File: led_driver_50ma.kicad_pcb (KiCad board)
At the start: 2 copper layers, 16 x 22.5 mm, 6 parts, among them J1 USB Micro B, J2 Screw_Terminal_01x02, SW2 Slide Switch

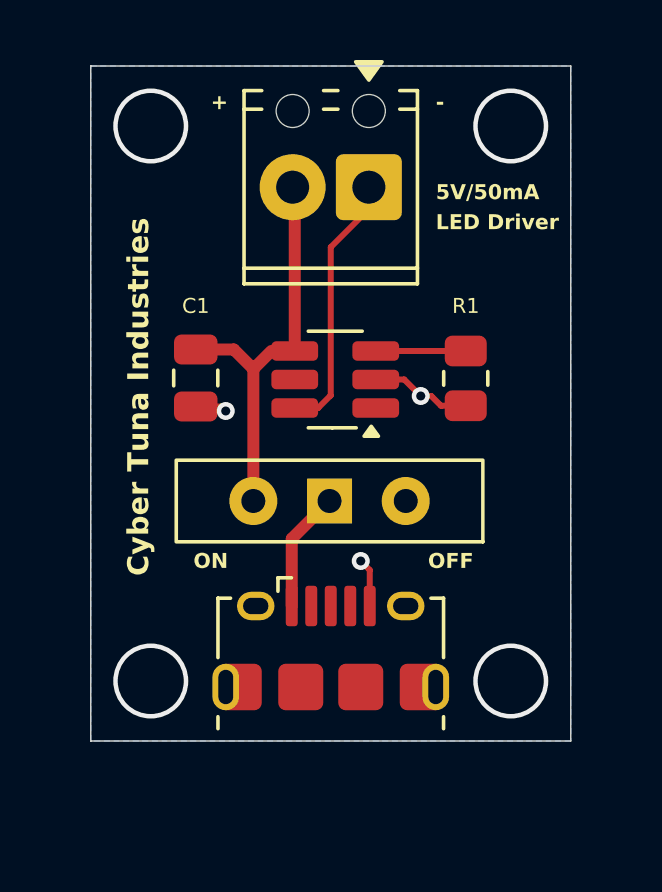
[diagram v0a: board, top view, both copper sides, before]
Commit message: Use bottom layer ground pour and few other tweaks
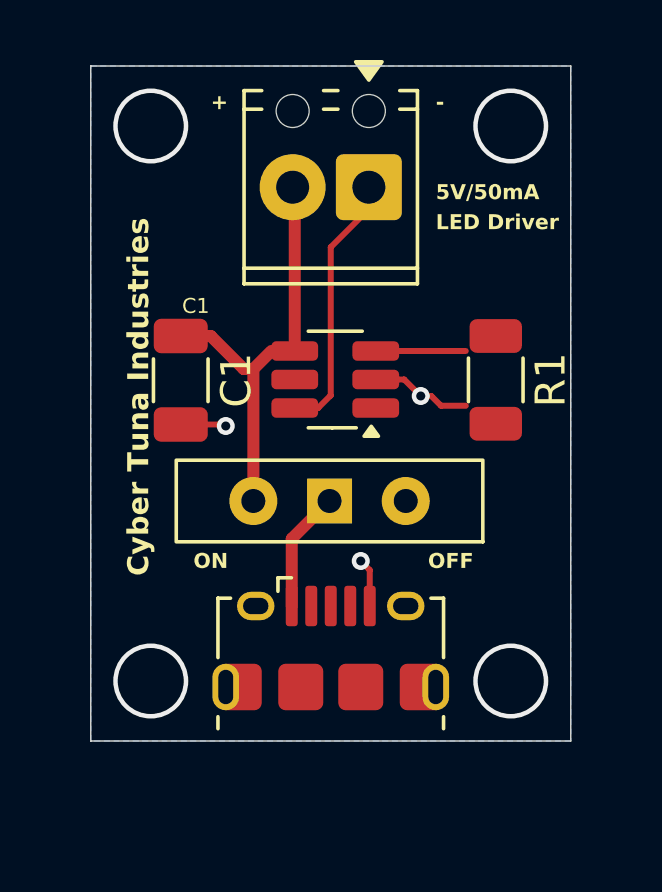
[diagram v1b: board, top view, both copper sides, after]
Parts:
- C1: footprint Capacitor_SMD:C_0805_2012Metric -> Capacitor_SMD:C_1206_3216Metric
- R1: footprint Resistor_SMD:R_0805_2012Metric -> Resistor_SMD:R_1206_3216Metric
- U1: value ~ -> AL5819
- moved R1 1.00 mm to (142.0, 104.5)
- moved C1 0.51 mm to (131.5, 104.5)
- renumbered SW2 to SW1
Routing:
- net +5V: track 13.4 -> 14.1 mm
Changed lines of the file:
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@@
 	(net 10 "unconnected-(U1-NC-Pad5)")
 	(net 11 "Net-(J1-VBUS)")
-	(net 12 "unconnected-(SW2-C-Pad2)")
+	(net 12 "unconnected-(SW1-C-Pad2)")
 	(footprint "Connector_USB:USB_Micro-B_Amphenol_10118194-0001LF_Horizontal"
 		(layer "F.Cu")
@@
 			)
 		)
-		(property "Value" "~"
+		(property "Value" "AL5819"
 			(at 0 2.9 0)
 			(layer "F.Fab")
@@
 		)
 	)
-	(footprint "Resistor_SMD:R_0805_2012Metric"
-		(layer "F.Cu")
-		(at 141 104.4125 -90)
-		(descr "Resistor SMD 0805 (2012 Metric), square (rectangular) end terminal, IPC-7351 nominal, (Body size source: IPC-SM-782 page 72, https://www.pcb-3d.com/wordpress/wp-content/uploads/ipc-sm-782a_amendment_1_and_2.pdf), generated with kicad-footprint-generator")
+	(footprint "Resistor_SMD:R_1206_3216Metric"
+		(layer "F.Cu")
+		(at 142 104.4625 -90)
+		(descr "Resistor SMD 1206 (3216 Metric), square (rectangular) end terminal, IPC-7351 nominal, (Body size source: IPC-SM-782 page 72, https://www.pcb-3d.com/wordpress/wp-content/uploads/ipc-sm-782a_amendment_1_and_2.pdf), generated with kicad-footprint-generator")
 		(tags "resistor")
 		(property "Reference" "R1"
-			(at -2.4125 0 180)
-			(layer "F.SilkS")
-			(effects
-				(font
-					(size 0.5 0.5)
-					(thickness 0.0625)
+			(at 0 -1.83 270)
+			(layer "F.SilkS")
+			(effects
+				(font
+					(size 1 1)
+					(thickness 0.15)
 				)
 			)
 		)
 		(property "Value" "30K"
-			(at 0 1.65 90)
-			(layer "F.Fab")
-			(hide yes)
+			(at 0 1.83 270)
+			(layer "F.Fab")
 			(effects
 				(font
@@
 		)
 		(property "Datasheet" "~"
-			(at 0 0 90)
+			(at 0 0 270)
 			(layer "F.Fab")
 			(hide yes)
@@
 		)
 		(property "Description" "Resistor, US symbol"
-			(at 0 0 90)
+			(at 0 0 270)
 			(layer "F.Fab")
 			(hide yes)
@@
 		(attr smd)
 		(fp_line
-			(start -0.227064 0.735)
-			(end 0.227064 0.735)
-			(stroke
-				(width 0.12)
-				(type solid)
-			)
-			(layer "F.SilkS")
-		)
-		(fp_line
-			(start -0.227064 -0.735)
-			(end 0.227064 -0.735)
+			(start -0.727064 0.91)
+			(end 0.727064 0.91)
+			(stroke
+				(width 0.12)
+				(type solid)
+			)
+			(layer "F.SilkS")
+		)
+		(fp_line
+			(start -0.727064 -0.91)
+			(end 0.727064 -0.91)
 			(stroke
 				(width 0.12)
@@
 		)
 		(fp_rect
-			(start -1.68 -0.95)
-			(end 1.68 0.95)
+			(start -2.28 -1.13)
+			(end 2.28 1.13)
 			(stroke
 				(width 0.05)
@@
 		)
 		(fp_rect
-			(start -1 -0.625)
-			(end 1 0.625)
+			(start -1.6 -0.8)
+			(end 1.6 0.8)
 			(stroke
 				(width 0.1)
@@
 		)
 		(fp_text user "${REFERENCE}"
-			(at 0 0 90)
-			(layer "F.Fab")
-			(effects
-				(font
-					(size 0.5 0.5)
-					(thickness 0.08)
+			(at 0 0 270)
+			(layer "F.Fab")
+			(effects
+				(font
+					(size 0.8 0.8)
+					(thickness 0.12)
 				)
 			)
 		)
 		(pad "1" smd roundrect
-			(at -0.9125 0 270)
-			(size 1.025 1.4)
-			(layers "F.Cu" "F.Mask" "F.Paste")
-			(roundrect_rratio 0.243902)
+			(at -1.4625 0 270)
+			(size 1.125 1.75)
+			(layers "F.Cu" "F.Mask" "F.Paste")
+			(roundrect_rratio 0.222222)
 			(net 8 "Net-(U1-R_{SET})")
 			(pintype "passive")
 		)
 		(pad "2" smd roundrect
-			(at 0.9125 0 270)
-			(size 1.025 1.4)
-			(layers "F.Cu" "F.Mask" "F.Paste")
-			(roundrect_rratio 0.243902)
+			(at 1.4625 0 270)
+			(size 1.125 1.75)
+			(layers "F.Cu" "F.Mask" "F.Paste")
+			(roundrect_rratio 0.222222)
 			(net 1 "GND")
 			(pintype "passive")
 		)
 		(embedded_fonts no)
-		(model "${KICAD9_3DMODEL_DIR}/Resistor_SMD.3dshapes/R_0805_2012Metric.step"
+		(model "${KICAD9_3DMODEL_DIR}/Resistor_SMD.3dshapes/R_1206_3216Metric.step"
 			(offset
 				(xyz 0 0 0)
@@
 		(descr "Wuerth, WS-SLTV, 450301014042, https://www.we-online.com/components/products/datasheet/450301014042.pdf")
 		(tags "switch single-pole opposite-side-connection double-throw SPDT würth wurth")
-		(property "Reference" "SW2"
+		(property "Reference" "SW1"
 			(at 5.96 -5 0)
 			(layer "F.SilkS")
@@
 			(layers "*.Cu" "*.Mask")
 			(remove_unused_layers no)
-			(net 12 "unconnected-(SW2-C-Pad2)")
+			(net 12 "unconnected-(SW1-C-Pad2)")
 			(pinfunction "C")
 			(pintype "passive")
@@
 		)
 	)
-	(footprint "Capacitor_SMD:C_0805_2012Metric"
-		(layer "F.Cu")
-		(at 132 104.4 -90)
-		(descr "Capacitor SMD 0805 (2012 Metric), square (rectangular) end terminal, IPC-7351 nominal, (Body size source: IPC-SM-782 page 76, https://www.pcb-3d.com/wordpress/wp-content/uploads/ipc-sm-782a_amendment_1_and_2.pdf, https://docs.google.com/spreadsheets/d/1BsfQQcO9C6DZCsRaXUlFlo91Tg2WpOkGARC1WS5S8t0/edit?usp=sharing), generated with kicad-footprint-generator")
+	(footprint "Capacitor_SMD:C_1206_3216Metric"
+		(layer "F.Cu")
+		(at 131.5 104.475 -90)
+		(descr "Capacitor SMD 1206 (3216 Metric), square (rectangular) end terminal, IPC-7351 nominal, (Body size source: IPC-SM-782 page 76, https://www.pcb-3d.com/wordpress/wp-content/uploads/ipc-sm-782a_amendment_1_and_2.pdf), generated with kicad-footprint-generator")
 		(tags "capacitor")
 		(property "Reference" "C1"
-			(at -2.9 0 90)
-			(layer "F.SilkS")
-			(hide yes)
+			(at 0 -1.85 270)
+			(layer "F.SilkS")
 			(effects
 				(font
@@
 		)
 		(property "Value" "1uF"
-			(at 0 1.68 90)
-			(layer "F.Fab")
-			(hide yes)
+			(at 0 1.85 270)
+			(layer "F.Fab")
 			(effects
 				(font
@@
 		)
 		(property "Datasheet" ""
-			(at 0 0 90)
+			(at 0 0 270)
 			(layer "F.Fab")
 			(hide yes)
@@
 		)
 		(property "Description" "capacitor, small US symbol"
-			(at 0 0 90)
+			(at 0 0 270)
 			(layer "F.Fab")
 			(hide yes)
@@
 		(attr smd)
 		(fp_line
-			(start -0.261252 0.735)
-			(end 0.261252 0.735)
-			(stroke
-				(width 0.12)
-				(type solid)
-			)
-			(layer "F.SilkS")
-		)
-		(fp_line
-			(start -0.261252 -0.735)
-			(end 0.261252 -0.735)
+			(start -0.711252 0.91)
+			(end 0.711252 0.91)
+			(stroke
+				(width 0.12)
+				(type solid)
+			)
+			(layer "F.SilkS")
+		)
+		(fp_line
+			(start -0.711252 -0.91)
+			(end 0.711252 -0.91)
 			(stroke
 				(width 0.12)
@@
 		)
 		(fp_rect
-			(start -1.7 -0.98)
-			(end 1.7 0.98)
+			(start -2.3 -1.15)
+			(end 2.3 1.15)
 			(stroke
 				(width 0.05)
@@
 		)
 		(fp_rect
-			(start -1 -0.625)
-			(end 1 0.625)
+			(start -1.6 -0.8)
+			(end 1.6 0.8)
 			(stroke
 				(width 0.1)
@@
 		)
 		(fp_text user "${REFERENCE}"
-			(at 0 0 90)
-			(layer "F.Fab")
-			(effects
-				(font
-					(size 0.5 0.5)
-					(thickness 0.08)
+			(at 0 0 270)
+			(layer "F.Fab")
+			(effects
+				(font
+					(size 0.8 0.8)
+					(thickness 0.12)
 				)
 			)
 		)
 		(pad "1" smd roundrect
-			(at -0.95 0 270)
-			(size 1 1.45)
-			(layers "F.Cu" "F.Mask" "F.Paste")
-			(roundrect_rratio 0.25)
+			(at -1.475 0 270)
+			(size 1.15 1.8)
+			(layers "F.Cu" "F.Mask" "F.Paste")
+			(roundrect_rratio 0.217391)
 			(net 3 "+5V")
 			(pintype "passive")
 		)
 		(pad "2" smd roundrect
-			(at 0.95 0 270)
-			(size 1 1.45)
-			(layers "F.Cu" "F.Mask" "F.Paste")
-			(roundrect_rratio 0.25)
+			(at 1.475 0 270)
+			(size 1.15 1.8)
+			(layers "F.Cu" "F.Mask" "F.Paste")
+			(roundrect_rratio 0.217391)
 			(net 1 "GND")
 			(pintype "passive")
 		)
 		(embedded_fonts no)
-		(model "${KICAD9_3DMODEL_DIR}/Capacitor_SMD.3dshapes/C_0805_2012Metric.step"
+		(model "${KICAD9_3DMODEL_DIR}/Capacitor_SMD.3dshapes/C_1206_3216Metric.step"
 			(offset
 				(xyz 0 0 0)
@@
 	)
 	(segment
-		(start 132.85 105.35)
-		(end 133 105.5)
+		(start 132.95 105.95)
+		(end 133 106)
 		(width 0.2)
 		(layer "F.Cu")
@@
 	)
 	(segment
-		(start 132 105.35)
-		(end 132.85 105.35)
-		(width 0.2)
-		(layer "F.Cu")
-		(net 1)
-	)
-	(segment
 		(start 138.95 104.45)
 		(end 138 104.45)
@@
 		(net 1)
 	)
+	(segment
+		(start 131.5 105.95)
+		(end 132.95 105.95)
+		(width 0.2)
+		(layer "F.Cu")
+		(net 1)
+	)
 	(via
-		(at 133 105.5)
+		(at 133 106)
 		(size 0.6)
 		(drill 0.3)
@@
 	)
 	(segment
+		(start 133.92 104.100001)
+		(end 133.600001 104.100001)
+		(width 0.4)
+		(layer "F.Cu")
+		(net 3)
+	)
+	(segment
 		(start 134.520001 103.5)
 		(end 135.3 103.5)
@@
 	)
 	(segment
-		(start 133.92 104.100001)
-		(end 133.269999 103.45)
-		(width 0.4)
-		(layer "F.Cu")
-		(net 3)
-	)
-	(segment
-		(start 133.269999 103.45)
-		(end 132 103.45)
-		(width 0.4)
-		(layer "F.Cu")
-		(net 3)
-	)
-	(segment
 		(start 135.3 98.7)
 		(end 135.46 98.54)
@@
 		(width 0.4)
 		(layer "F.Cu")
+		(net 3)
+	)
+	(segment
+		(start 133.600001 104.100001)
+		(end 132.5 103)
+		(width 0.4)
+		(layer "F.Cu")
+		(net 3)
+	)
+	(segment
+		(start 132.5 103)
+		(end 131.5 103)
+		(width 0.4)
+		(layer "F.Cu")

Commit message: switch to USB c instead of usb micro
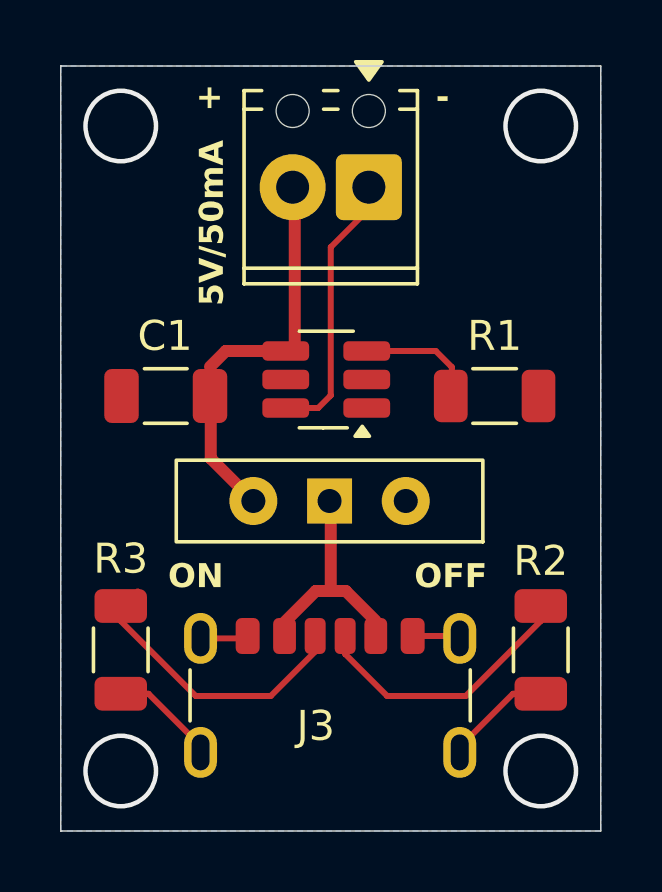
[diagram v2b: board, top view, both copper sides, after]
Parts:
- removed J1: USB Micro B, Connector_USB:USB_Micro-B_Amphenol_10118194-0001LF_Horizontal
- added J3: USB C Receptacle, Connector_USB:USB_C_Receptacle_GCT_USB4125-xx-x_6P_TopMnt_Horizontal, F.Cu at (136.5, 116.1)
- added R2: 5.1K, Resistor_SMD:R_1206_3216Metric, F.Cu at (143.5, 113.5)
- added R3: 5.1K, Resistor_SMD:R_1206_3216Metric, F.Cu at (129.5, 113.5)
- moved C1 0.73 mm to (131.0, 105.0), turned to 180 degrees
- moved R1 0.54 mm to (142.0, 105.0), turned to 0 degrees
- moved U1 0.30 mm to (136.3, 104.5)
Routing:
- net Net-(J3-CC1): track 0.00 -> 9.94 mm
- net Net-(J3-CC2): track 0.00 -> 9.24 mm
- net GND: track 6.51 -> 10.9 mm, vias 3 -> 0
- net Net-(SW1-B): track 4.02 -> 7.86 mm
- net Net-(U1-R_{SET}): track 3.00 -> 3.72 mm
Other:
- board size 16 x 22.5 mm -> 18 x 25.5 mm
- board text removed: "C1"
- board text removed: "LED Driver"

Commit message: finished making some connections
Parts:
- moved J2 0.50 mm to (137.8, 98.5)
- moved R2 0.50 mm to (143.5, 113.0)
- moved R3 0.50 mm to (129.5, 113.0)
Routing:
- net GND: track 10.9 -> 16.4 mm, vias 0 -> 3
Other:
- board size 18 x 25.5 mm -> 18 x 24.5 mm
- board text added: "5V/ 50mA"
- board text removed: "5V/50mA"
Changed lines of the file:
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@@
 	(footprint "Resistor_SMD:R_1206_3216Metric"
 		(layer "F.Cu")
-		(at 143.5 113.4625 -90)
+		(at 143.5 112.9625 -90)
 		(descr "Resistor SMD 1206 (3216 Metric), square (rectangular) end terminal, IPC-7351 nominal, (Body size source: IPC-SM-782 page 72, https://www.pcb-3d.com/wordpress/wp-content/uploads/ipc-sm-782a_amendment_1_and_2.pdf), generated with kicad-footprint-generator")
 		(tags "resistor")
@@
 	(footprint "TerminalBlock_Phoenix:TerminalBlock_Phoenix_MPT-0,5-2-2.54_1x02_P2.54mm_Horizontal"
 		(layer "F.Cu")
-		(at 137.77 98.04 180)
+		(at 137.77 98.54 180)
 		(descr "Terminal Block Phoenix MPT-0,5-2-2.54, 2 pins, pitch 2.54mm, size 5.54x6.2mm, drill diameter 1.1mm, pad diameter 2.2mm, http://www.mouser.com/ds/2/324/ItemDetail_1725656-920552.pdf, script-generated using https://gitlab.com/kicad/libraries/kicad-footprint-generator/-/tree/master/scripts/TerminalBlock_Phoenix")
 		(tags "THT Terminal Block Phoenix MPT-0,5-2-2.54 pitch 2.54mm size 5.54x6.2mm drill 1.1mm pad 2.2mm")
@@
 	(footprint "Resistor_SMD:R_1206_3216Metric"
 		(layer "F.Cu")
-		(at 129.5 113.4625 -90)
+		(at 129.5 112.9625 -90)
 		(descr "Resistor SMD 1206 (3216 Metric), square (rectangular) end terminal, IPC-7351 nominal, (Body size source: IPC-SM-782 page 72, https://www.pcb-3d.com/wordpress/wp-content/uploads/ipc-sm-782a_amendment_1_and_2.pdf), generated with kicad-footprint-generator")
 		(tags "resistor")
@@
 	)
 	(gr_rect
-		(start 127.5 94)
+		(start 127.5 95)
 		(end 145.5 119.5)
 		(stroke
@@
 	)
 	(gr_text "+"
-		(at 132 95.5 0)
+		(at 132 96.5 0)
 		(layer "F.SilkS")
 		(effects
@@
 	)
 	(gr_text "-"
-		(at 140 95.5 0)
+		(at 140 96.5 0)
 		(layer "F.SilkS")
 		(effects
@@
 		)
 	)
-	(gr_text "5V/50mA"
-		(at 133 102 90)
+	(gr_text "5V/\n50mA"
+		(at 131 101 0)
 		(layer "F.SilkS")
 		(effects
@@
 				(bold yes)
 			)
-			(justify left bottom)
+			(justify bottom)
 		)
 	)
 	(gr_text "Cyber Tuna Industries"
-		(at 130 100 90)
+		(at 143.5 113.5 270)
 		(layer "B.SilkS")
 		(effects
@@
 	)
 	(via
-		(at 129.5 96)
+		(at 129.5 97)
 		(size 2.5)
 		(drill 2.2)
@@
 	)
 	(via
-		(at 143.5 96)
+		(at 143.5 97)
 		(size 2.5)
 		(drill 2.2)
@@
 	)
 	(segment
+		(start 137.75 104.5)
+		(end 137.7 104.45)
+		(width 0.2)
+		(layer "F.Cu")
+		(net 1)
+	)
+	(segment
 		(start 132 112.92)
 		(end 132.16 113.08)
@@
 	)
 	(segment
+		(start 129.5 107)
+		(end 129.5 105.025)
+		(width 0.2)
+		(layer "F.Cu")
+		(net 1)
+	)
+	(segment
 		(start 133.65 113.08)
 		(end 133.73 113)
@@
 	)
 	(segment
-		(start 130.425 114.925)
-		(end 129.5 114.925)
+		(start 139 104.5)
+		(end 137.75 104.5)
+		(width 0.2)
+		(layer "F.Cu")
+		(net 1)
+	)
+	(segment
+		(start 129.925 114.425)
+		(end 129.5 114.425)
 		(width 0.2)
 		(layer "F.Cu")
@@
 	)
 	(segment
+		(start 143.5 105.075)
+		(end 143.425 105)
+		(width 0.2)
+		(layer "F.Cu")
+		(net 1)
+	)
+	(segment
 		(start 140.72 113)
 		(end 140.8 113.08)
@@
 	(segment
 		(start 132.16 116.66)
-		(end 130.425 114.925)
+		(end 129.925 114.425)
 		(width 0.2)
 		(layer "F.Cu")
@@
 	)
 	(segment
+		(start 142.5 106.5)
+		(end 143.5 105.5)
+		(width 0.2)
+		(layer "F.Cu")
+		(net 1)
+	)
+	(segment
 		(start 132.16 116.88)
 		(end 132.16 116.66)
@@
 	)
 	(segment
+		(start 143.5 105.5)
+		(end 143.5 105.075)
+		(width 0.2)
+		(layer "F.Cu")
+		(net 1)
+	)
+	(segment
+		(start 129.5 105.025)
+		(end 129.525 105)
+		(width 0.2)
+		(layer "F.Cu")
+		(net 1)
+	)
+	(segment
 		(start 140.8 116.7)
 		(end 142.575 114.925)
 		(width 0.2)
 		(layer "F.Cu")
+		(net 1)
+	)
+	(via
+		(at 139 104.5)
+		(size 0.6)
+		(drill 0.3)
+		(layers "F.Cu" "B.Cu")
+		(free yes)
+		(net 1)
+	)
+	(via
+		(at 129.5 107)
+		(size 0.6)
+		(drill 0.3)
+		(layers "F.Cu" "B.Cu")
+		(free yes)
+		(net 1)
+	)
+	(via
+		(at 142.5 106.5)
+		(size 0.6)
+		(drill 0.3)
+		(layers "F.Cu" "B.Cu")
+		(free yes)
 		(net 1)
 	)
@@
 	)
 	(segment
+		(start 132.475 104.025)
+		(end 132.475 105)
+		(width 0.4)
+		(layer "F.Cu")
+		(net 3)
+	)
+	(segment
 		(start 135.3 98.11)
 		(end 135.23 98.04)
@@
 	)
 	(segment
-		(start 132.475 105)
-		(end 132.475 104.025)
-		(width 0.2)
-		(layer "F.Cu")
-		(net 3)
-	)
-	(segment
 		(start 135.25 103.45)
 		(end 135.3 103.5)
@@
 	)
 	(segment
-		(start 140.5375 105)
-		(end 140.5375 104.0375)
-		(width 0.2)
-		(layer "F.Cu")
-		(net 4)
-	)
-	(segment
-		(start 140.5375 104.0375)
-		(end 140 103.5)
+		(start 140 103.5)
+		(end 140.5 104)
 		(width 0.2)
 		(layer "F.Cu")
@@
 	)
 	(segment
-		(start 136.5 111.5)
+		(start 140.5 104)
+		(end 140.5 105)
+		(width 0.2)
+		(layer "F.Cu")
+		(net 4)
+	)
+	(segment
+		(start 136.5 111)
 		(end 136.5 108.54)
 		(width 0.4)
@@
 	)
 	(segment
-		(start 137 111.5)
-		(end 136.5 111.5)
+		(start 136.5 111)
+		(end 134.96 112.54)
 		(width 0.4)
 		(layer "F.Cu")
@@
 	)
 	(segment
-		(start 136 111.5)
-		(end 134.96 112.54)
+		(start 138 112.5)
+		(end 136.5 111)
 		(width 0.4)
 		(layer "F.Cu")
@@
 	)
 	(segment
-		(start 138 112.5)
-		(end 137 111.5)
-		(width 0.4)
-		(layer "F.Cu")
-		(net 8)
-	)
-	(segment
-		(start 136.5 111.5)
-		(end 136 111.5)
-		(width 0.4)
-		(layer "F.Cu")
-		(net 8)
+		(start 136.98 113)
+		(end 136.98 113.48)
+		(width 0.2)
+		(layer "F.Cu")
+		(net 9)
 	)
 	(segment
@@
 	)
 	(segment
-		(start 138.38 115)
+		(start 136.98 113.48)
+		(end 138.5 115)
+		(width 0.2)
+		(layer "F.Cu")
+		(net 9)
+	)
+	(segment
+		(start 138.5 115)
 		(end 141 115)
-		(width 0.2)
-		(layer "F.Cu")
-		(net 9)
-	)
-	(segment
-		(start 136.98 113)
-		(end 136.98 113.6)
-		(width 0.2)
-		(layer "F.Cu")
-		(net 9)
-	)
-	(segment
-		(start 136.98 113.6)
-		(end 138.38 115)
 		(width 0.2)
 		(layer "F.Cu")
@@
 		(polygon
 			(pts
-				(xy 127.5 94) (xy 145.5 94) (xy 145.5 119.5) (xy 127.5 119.5)
-			)
-		)
+				(xy 127.5 95) (xy 145.5 95) (xy 145.5 119.5) (xy 127.5 119.5)
+			)
+		)
